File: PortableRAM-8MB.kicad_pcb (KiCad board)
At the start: 4 copper layers, 123 x 81 mm, 38 parts, among them J1 RAM Connector, J2 JTAG_Header_2.54mm_1x06, U1 ATF1502ASL, U11 74HC245, U12 74HC245, U2 AS6C8008-55ZIN, U3 AS6C8008-55ZIN, U4 AS6C8008-55ZIN, U5 AS6C8008-55ZIN, U6 AS6C8008-55ZIN, U7 AS6C8008-55ZIN, U8 AS6C8008-55ZIN, U9 AS6C8008-55ZIN

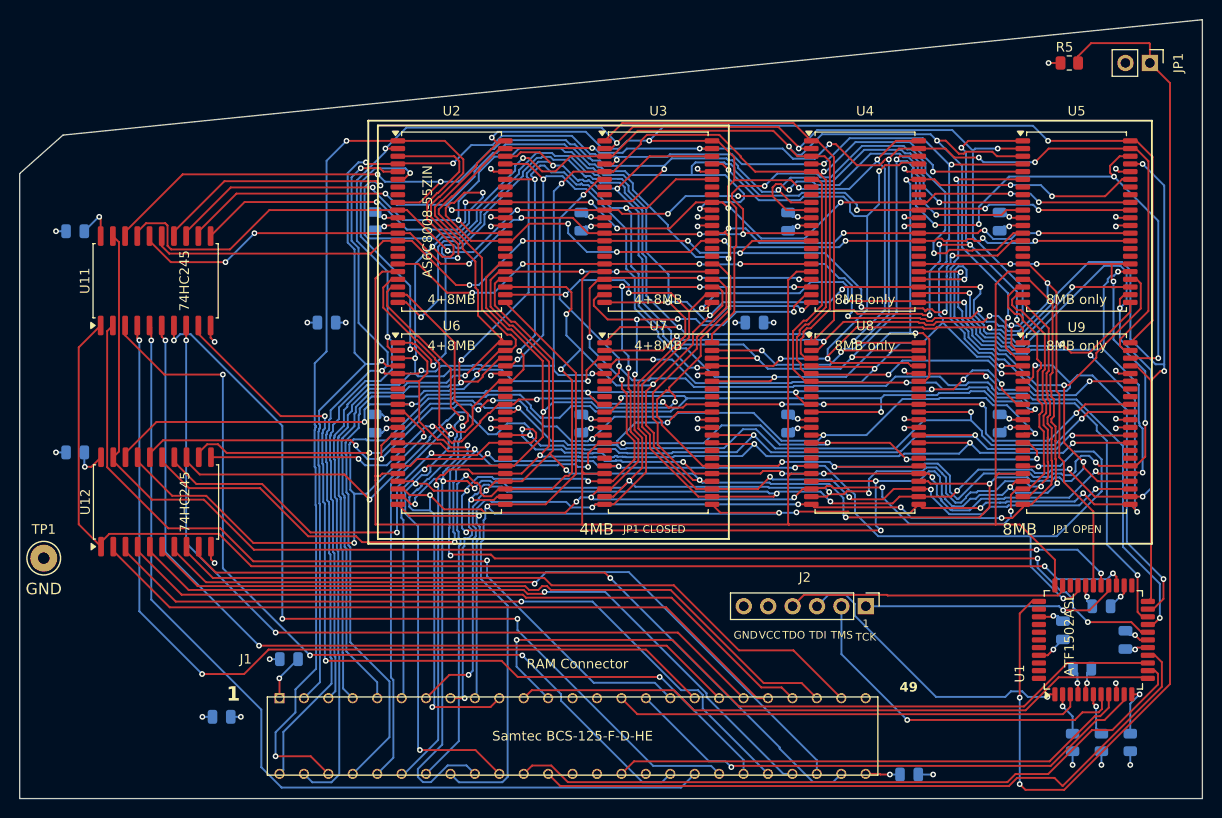
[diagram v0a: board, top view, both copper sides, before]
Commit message: v3 board: MODEL jumper, bank LEDs, pull-down resistors, sequential population
- MODEL jumper (JP1): open=M5120 full 8MB, closed=M5126 cap at 6MB to
  avoid SLOT_CS0 conflict with backlit display controller
- 4 green latching LEDs (D1–D4) — CPLD registered macrocell latches ON
  when each 2MB bank is confirmed at boot; power-cycle clears
- 16× 10KΩ pull-downs (R5–R20) on SD0–SD15 to prevent ghost RAM reads
  on unpopulated banks
- Sequential bank population: U1+U5=2MB, U2+U6=4MB, U3+U7=6MB, U4+U8=8MB
  (no SIZE jumper needed)
- Firmware recompiled for v3 (WinCUPL + Wine, prjbureau SVF) 2026-07-17
- Gerbers regenerated after component renumbering
- README rewritten for v3 features and new designators

Co-Authored-By: Claude Sonnet 4.6 <noreply@anthropic.com>
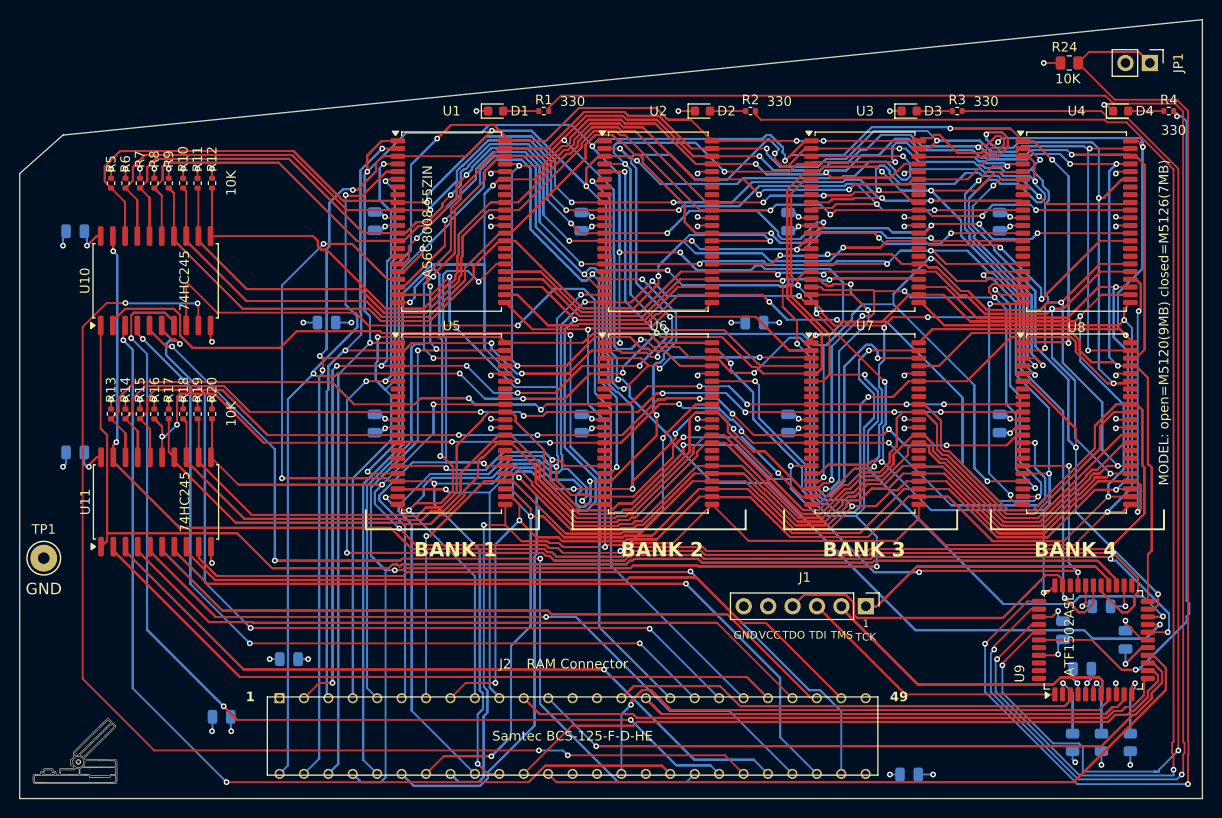
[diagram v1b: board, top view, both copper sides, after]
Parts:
- added D1: GREEN, LED_SMD:LED_0603_1608Metric, F.Cu at (118.0, 78.5)
- added D2: GREEN, LED_SMD:LED_0603_1608Metric, F.Cu at (139.5, 78.5)
- added D3: GREEN, LED_SMD:LED_0603_1608Metric, F.Cu at (161.0, 78.5)
- added D4: GREEN, LED_SMD:LED_0603_1608Metric, F.Cu at (183.0, 78.5)
- added R1: 330, Resistor_SMD:R_0402_1005Metric, F.Cu at (123.0, 78.5)
- added R10: 10K, Resistor_SMD:R_0402_1005Metric, F.Cu at (85.5, 86.0)
- added R11: 10K, Resistor_SMD:R_0402_1005Metric, F.Cu at (87.0, 86.0)
- added R12: 10K, Resistor_SMD:R_0402_1005Metric, F.Cu at (88.5, 86.0)
- added R13: 10K, Resistor_SMD:R_0402_1005Metric, F.Cu at (78.0, 110.0)
- added R14: 10K, Resistor_SMD:R_0402_1005Metric, F.Cu at (79.5, 110.0)
- added R15: 10K, Resistor_SMD:R_0402_1005Metric, F.Cu at (81.0, 110.0)
- added R16: 10K, Resistor_SMD:R_0402_1005Metric, F.Cu at (82.5, 110.0)
- added R17: 10K, Resistor_SMD:R_0402_1005Metric, F.Cu at (84.0, 110.0)
- added R18: 10K, Resistor_SMD:R_0402_1005Metric, F.Cu at (85.5, 110.0)
- added R19: 10K, Resistor_SMD:R_0402_1005Metric, F.Cu at (87.0, 110.0)
- added R2: 330, Resistor_SMD:R_0402_1005Metric, F.Cu at (144.5, 78.5)
- added R20: 10K, Resistor_SMD:R_0402_1005Metric, F.Cu at (88.5, 110.0)
- added R3: 330, Resistor_SMD:R_0402_1005Metric, F.Cu at (166.0, 78.5)
- added R4: 330, Resistor_SMD:R_0402_1005Metric, F.Cu at (188.0, 78.5)
- added R5: 10K, Resistor_SMD:R_0402_1005Metric, F.Cu at (78.0, 86.0)
- added R6: 10K, Resistor_SMD:R_0402_1005Metric, F.Cu at (79.5, 86.0)
- added R7: 10K, Resistor_SMD:R_0402_1005Metric, F.Cu at (81.0, 86.0)
- added R8: 10K, Resistor_SMD:R_0402_1005Metric, F.Cu at (82.5, 86.0)
- added R9: 10K, Resistor_SMD:R_0402_1005Metric, F.Cu at (84.0, 86.0)
- JP1: value JP1: open=8MB closed=4MB -> MODEL: open=M5120(9MB) closed=M5126(7MB)
- renumbered C4 to C1, C12 to C10, C9 to C11, C18 to C12, C10 to C13, C17 to C14, C14 to C15, C19 to C16, C13 to C17, C15 to C18, C16 to C19, C3 to C2, C2 to C3, C1 to C4, C8 to C5, C7 to C6, C6 to C7, C5 to C8, C11 to C9, J2 to J1, J1 to J2, R3 to R21, R2 to R22, R4 to R23, R5 to R24, U2 to U1, U11 to U10, U12 to U11, U3 to U2, U4 to U3, U5 to U4, U6 to U5, U7 to U6, U8 to U7, U9 to U8, U1 to U9
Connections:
- net /SIZE8 renamed /MODEL
- U9 pad 35: unconnected-(U1-I/O/GCLK3-Pad35) -> /LED0
- U9 pad 37: unconnected-(U1-I/GCLK1-Pad37) -> /LED1
- U9 pad 38: unconnected-(U1-I/OE1/Vpp-Pad38) -> /LED2
- U9 pad 39: unconnected-(U1-I/GCLR-Pad39) -> /LED3
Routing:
- net /A8: track 236.7 -> 499.3 mm, vias 11 -> 9
- net /A7: track 228.8 -> 489.5 mm, vias 9 -> 11
- net /A9: track 219.7 -> 474.9 mm, vias 11 -> 9
- net /SD15: track 105.8 -> 351.8 mm, vias 8 -> 5
- net /A3: track 238.4 -> 445.4 mm, vias 7 -> 12
- net /A13: track 213.5 -> 418.6 mm, vias 12 -> 5
- net /LDS: track 56.2 -> 252.9 mm, vias 1 -> 0
- net /A11: track 208.4 -> 390.3 mm, vias 12 -> 5
- net /A10: track 209.3 -> 385.7 mm, vias 10 -> 6
- net /LED0: track 0.00 -> 171.8 mm, vias 0 -> 2
- net /A1: track 220.2 -> 390.8 mm, vias 9 -> 10
- net /A17: track 215.6 -> 378.0 mm, vias 12 -> 10
- net /A4: track 213.4 -> 375.2 mm, vias 9 -> 11
- net /A5: track 281.4 -> 442.8 mm
- net /A2: track 213.7 -> 373.8 mm, vias 9 -> 14
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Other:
- board text added: "BANK 1"
- board text added: "BANK 2"
- board text added: "BANK 3"
- board text added: "BANK 4"
- board text added: "Mac Portable RAM Expansion Card v3"
- board text removed: "4+8MB"
- board text removed: "4MB"
- board text removed: "8MB"
- board text removed: "8MB only"
- board text removed: "JP1 CLOSED"
- board text removed: "JP1 OPEN"
- board text removed: "Mac Portable 8MB RAM Card v2.0"

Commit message: Fix CPLD LED pin assignments: move LED1/2/3 from dedicated input pins to valid I/O pins
Pins 37/38/39 on ATF1502ASL TQFP-44 are dedicated input-only pins with no output
driver. Declaring registered outputs (LED1/2/3) there caused the fitter to fail all
PREASSIGN=KEEP passes and fall back to IGNORE, scrambling every pin assignment.

- firmware/PortableRAM8.pld: LED1 pin 37->42, LED2 pin 38->43, LED3 pin 39->44
- PortableRAM-8MB.kicad_sch: reconnected LED1/2/3 nets to pins 42/43/44; X on 37/38/39
- PortableRAM-8MB.kicad_pcb: netlist updated, traces rerouted to pads 42/43/44
- firmware/PortableRAM8.jed/.fit/.svf: recompiled; fitter now succeeds PREASSIGN=KEEP

Co-Authored-By: Claude Sonnet 4.6 <noreply@anthropic.com>
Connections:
- U9 pad 37: /LED1 -> unconnected-(U9-I/GCLK1-Pad37)
- U9 pad 38: /LED2 -> unconnected-(U9-I/OE1/Vpp-Pad38)
- U9 pad 39: /LED3 -> unconnected-(U9-I/GCLR-Pad39)
- U9 pad 42: unconnected-(U1-I/O-Pad42) -> /LED1
- U9 pad 43: unconnected-(U1-I/O-Pad43) -> /LED2
- U9 pad 44: unconnected-(U1-I/O-Pad44) -> /LED3
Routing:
- net /LED3: track 87.2 -> 81.9 mm
- net /LED2: track 118.5 -> 116.3 mm
- net /LED1: track 140.7 -> 139.4 mm
- net unconnected-(U9-I/GCLK1-Pad37): track 0.00 -> 0.75 mm
- net unconnected-(U9-I/OE1/Vpp-Pad38): track 0.00 -> 0.56 mm

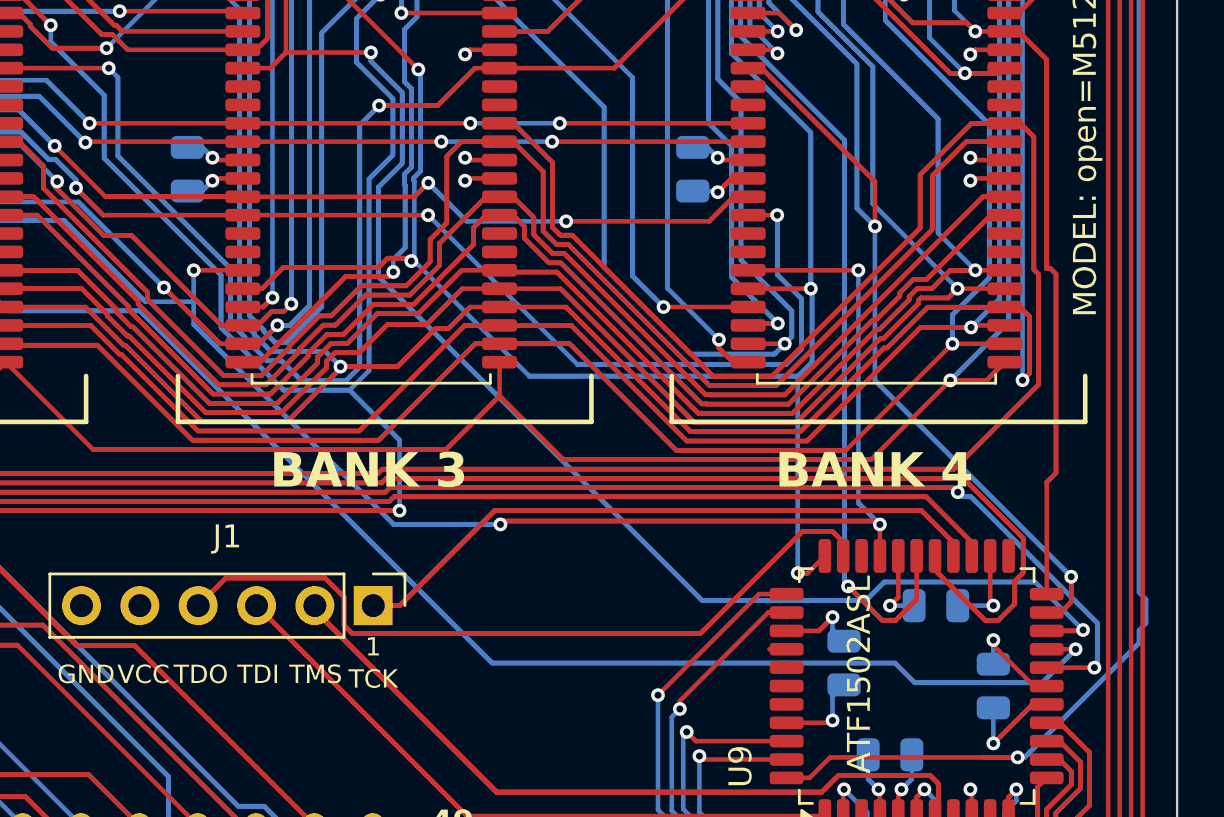
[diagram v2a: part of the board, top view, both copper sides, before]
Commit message: Add J3 PDS header (1x2, 2.54mm): DTACK→pin 23, EXT_DTACK→pin 31
Schematic: added Conn_01x02 J3 with nets DTACK_OUT/EXT_DTACK_OUT
wired to U9 CPLD pins 23 and 31. Removed no-connect markers from
those pads.

PCB: placed J3 on board edge, routed U9 pad 23→J3 pin 1 (DTACK)
and U9 pad 31→J3 pin 2 (EXT_DTACK). DRC clean: 0 errors,
0 unconnected pads.

User connects J3 pin 1 to PDS B7 (/DTACK) with a removable wire.
No more soldering to CPLD pads.

Co-Authored-By: Claude Sonnet 4.6 <noreply@anthropic.com>
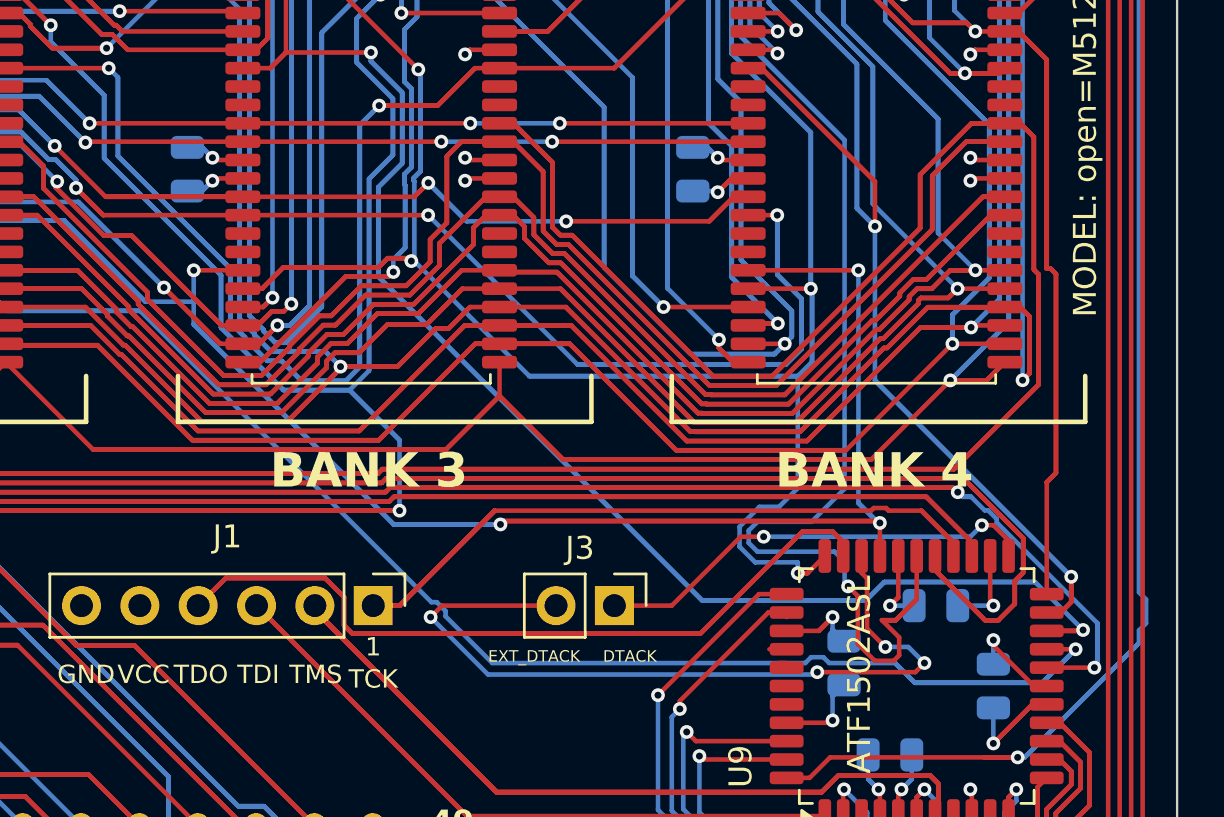
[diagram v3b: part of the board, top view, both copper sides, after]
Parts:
- added J3: PDS Header 1x2, Connector_PinHeader_2.54mm:PinHeader_1x02_P2.54mm_Vertical, F.Cu at (167.0, 130.0)
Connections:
- U9 pad 23: unconnected-(U9-I/O-Pad23) -> /DTACK_OUT
- U9 pad 31: unconnected-(U9-I/O-Pad31) -> /EXT_DTACK_OUT
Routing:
- net /CE1: track 183.7 -> 144.8 mm
- net /TCK: track 89.4 -> 52.4 mm
- net /EXT_DTACK_OUT: track 0.00 -> 34.8 mm, vias 0 -> 4
- net /DTACK_OUT: track 0.00 -> 19.6 mm, vias 0 -> 2
- net /WEL: track 235.1 -> 225.1 mm
- net /CE0: track 264.4 -> 256.7 mm
- net /BANKSEL: track 357.8 -> 361.5 mm
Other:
- board text added: "DTACK"
- board text added: "EXT_DTACK"

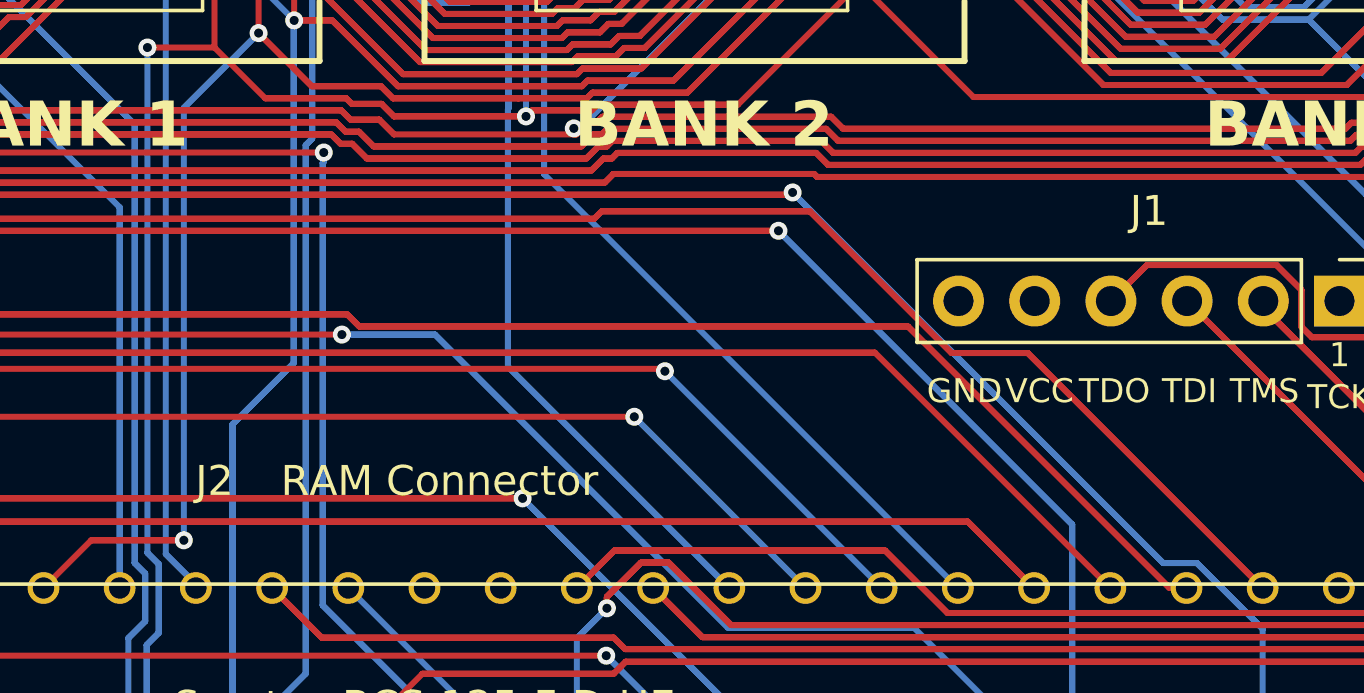
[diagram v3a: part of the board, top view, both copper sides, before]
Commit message: fix: swap J1↔J2 to match v2 convention; add J3 to BOM
v3 had J1=JTAG and J2=RAM connector — reversed from v2.
Correct convention (matching v2): J1=RAM connector (Samtec),
J2=JTAG header, J3=DTACK header.

Updated schematic, PCB, BOM CSV, and README throughout.
Also added missing J3 PDS DTACK header row to BOM CSV.

Co-Authored-By: Claude Sonnet 4.6 <noreply@anthropic.com>
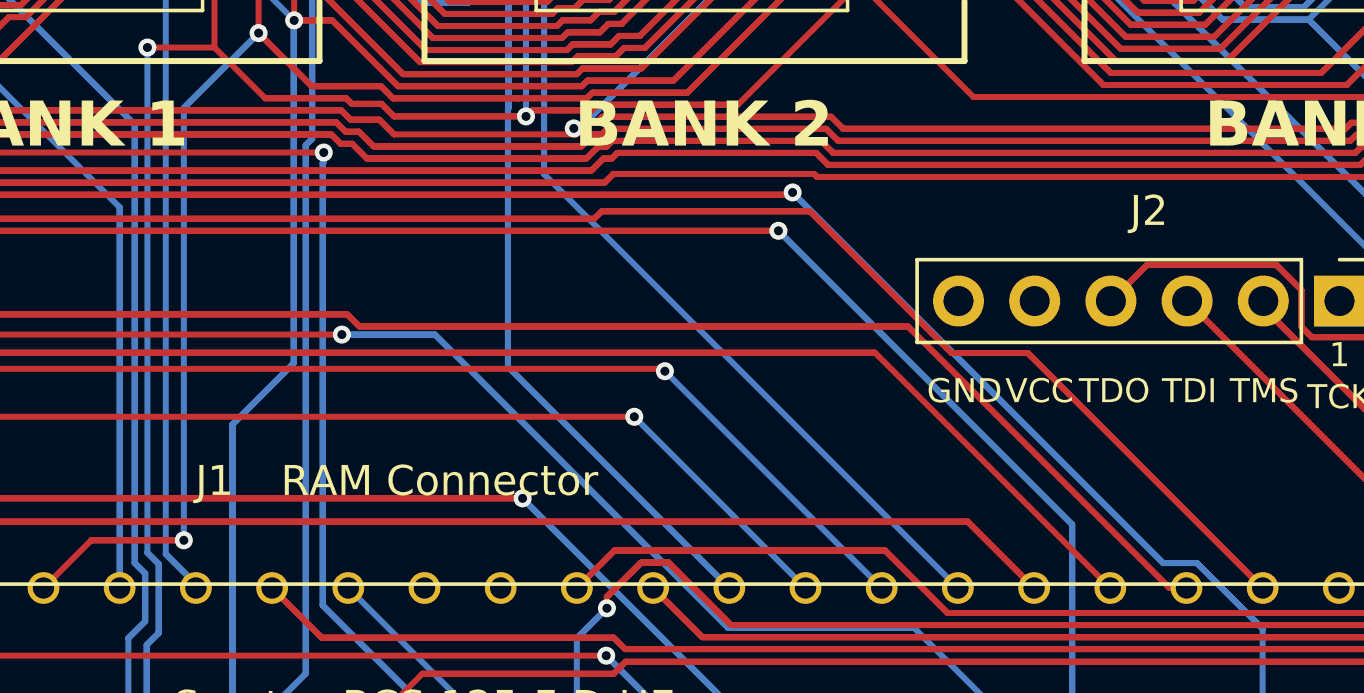
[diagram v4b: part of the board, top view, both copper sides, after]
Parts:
- renumbered J2 to J1, J1 to J2
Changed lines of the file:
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@@
 		(descr "Through hole straight pin header, 1x06, 2.54mm pitch, single row")
 		(tags "Through hole pin header THT 1x06 2.54mm single row")
-		(property "Reference" "J1"
+		(property "Reference" "J2"
 			(at -3 6.35 0)
 			(layer "F.SilkS")
@@
 		(descr "Samtec BCS-125-F-D-HE, 2x25 2.54mm through-hole connector")
 		(tags "connector samtec BCS 50pin 2x25 2.54mm through-hole")
-		(property "Reference" "J2"
+		(property "Reference" "J1"
 			(at 7 7.5 0)
 			(layer "F.SilkS")
